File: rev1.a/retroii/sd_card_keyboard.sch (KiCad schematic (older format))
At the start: 47 parts, among them CON1 SD_Card_SPI, J22 Conn_01x09, K1 PS2_KEYBOARD, P2 PROP_PLUG, Q5 2N3904, SW3 SAVE, SW4 LOAD, SW5 SW_PUSH_SAFE, SW6 RESET, SW7 MISC1, SW8 MISC2, U16 Prop_P8X32A, U17 24LC256_EEPROM, Y3 5MHz 20pf

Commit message: added tactile switches 3d models, footprints, symbols.
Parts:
- SW3, SW4, SW6, SW7, SW8: footprint (none) -> retroii_footprints:TE_Tactile_2-1825027-0; symbol Switch:SW_Push -> retroii:SW_Push
- SW5: footprint 6502Library:1-1825027-1-TACTILE_SWITCH -> retroii_footprints:TE_1825910-6; symbol 6502:SW_PUSH_SAFE -> retroii:SW_Push
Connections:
- wire segments 254 -> 256
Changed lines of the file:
@@
 NoConn ~ 2700 1700
 $Comp
-L 6502:SW_PUSH_SAFE SW5
+L retroii:SW_Push SW5
 U 1 1 5C8ADCC7
 P 3580 1455
 F 0 "SW5" H 3730 1565 50  0000 C CNN
 F 1 "SW_PUSH_SAFE" H 3580 1375 50  0000 C CNN
-F 2 "6502Library:1-1825027-1-TACTILE_SWITCH" H 3580 1455 60  0001 C CNN
+F 2 "retroii_footprints:TE_1825910-6" H 3580 1455 60  0001 C CNN
 F 3 "" H 3580 1455 60  0000 C CNN
 	1    3580 1455
@@
 ~Reset
 $Comp
-L Switch:SW_Push SW4
+L retroii:SW_Push SW4
 U 1 1 5D8FADA2
 P 1270 3375
 F 0 "SW4" H 1270 3325 50  0000 C CNN
 F 1 "LOAD" H 1270 3530 50  0000 C CNN
-F 2 "" H 1270 3575 50  0001 C CNN
+F 2 "retroii_footprints:TE_Tactile_2-1825027-0" H 1270 3575 50  0001 C CNN
 F 3 "~" H 1270 3575 50  0001 C CNN
 	1    1270 3375
@@
 $EndComp
 $Comp
-L Switch:SW_Push SW6
+L retroii:SW_Push SW6
 U 1 1 5D8FC47F
 P 3725 5450
 F 0 "SW6" H 3735 5385 50  0000 C CNN
 F 1 "RESET" H 3725 5605 50  0000 C CNN
-F 2 "" H 3725 5650 50  0001 C CNN
+F 2 "retroii_footprints:TE_Tactile_2-1825027-0" H 3725 5650 50  0001 C CNN
 F 3 "~" H 3725 5650 50  0001 C CNN
 	1    3725 5450
@@
 	1635 3375 1700 3375
 $Comp
-L Switch:SW_Push SW3
+L retroii:SW_Push SW3
 U 1 1 5CDC6D67
 P 1270 3980
 F 0 "SW3" H 1270 3930 50  0000 C CNN
 F 1 "SAVE" H 1270 4135 50  0000 C CNN
-F 2 "" H 1270 4180 50  0001 C CNN
+F 2 "retroii_footprints:TE_Tactile_2-1825027-0" H 1270 4180 50  0001 C CNN
 F 3 "~" H 1270 4180 50  0001 C CNN
 	1    1270 3980
@@
 	1635 3980 1700 3980
 $Comp
-L Switch:SW_Push SW7
+L retroii:SW_Push SW7
 U 1 1 5CE00EDA
 P 1270 4535
 F 0 "SW7" H 1270 4485 50  0000 C CNN
 F 1 "MISC1" H 1270 4690 50  0000 C CNN
-F 2 "" H 1270 4735 50  0001 C CNN
+F 2 "retroii_footprints:TE_Tactile_2-1825027-0" H 1270 4735 50  0001 C CNN
 F 3 "~" H 1270 4735 50  0001 C CNN
 	1    1270 4535
@@
 	1635 4535 1700 4535
 $Comp
-L Switch:SW_Push SW8
+L retroii:SW_Push SW8
 U 1 1 5CE00EF8
 P 1270 5140
 F 0 "SW8" H 1270 5090 50  0000 C CNN
 F 1 "MISC2" H 1270 5295 50  0000 C CNN
-F 2 "" H 1270 5340 50  0001 C CNN
+F 2 "retroii_footprints:TE_Tactile_2-1825027-0" H 1270 5340 50  0001 C CNN
 F 3 "~" H 1270 5340 50  0001 C CNN
 	1    1270 5140
@@
 NoConn ~ 5115 6835
 NoConn ~ 5115 6935
+Wire Wire Line
+	3380 1455 3280 1455
+Wire Wire Line
+	3780 1455 3880 1455
+Connection ~ 3880 1455
 Wire Bus Line
 	10725 2260 10725 5405

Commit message: finished footprints/models for power supply caps
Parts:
- C37: footprint 6502Library:C_Disc_D6_P5 -> Capacitor_THT:C_Disc_D4.7mm_W2.5mm_P5.00mm
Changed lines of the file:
@@
 F 0 "C37" H 8500 1610 50  0000 L CNN
 F 1 "1uf" H 8500 1460 50  0000 L CNN
-F 2 "6502Library:C_Disc_D6_P5" H 8490 1540 60  0001 C CNN
+F 2 "Capacitor_THT:C_Disc_D4.7mm_W2.5mm_P5.00mm" H 8490 1540 60  0001 C CNN
 F 3 "" H 8490 1540 60  0000 C CNN
 	1    8490 1540

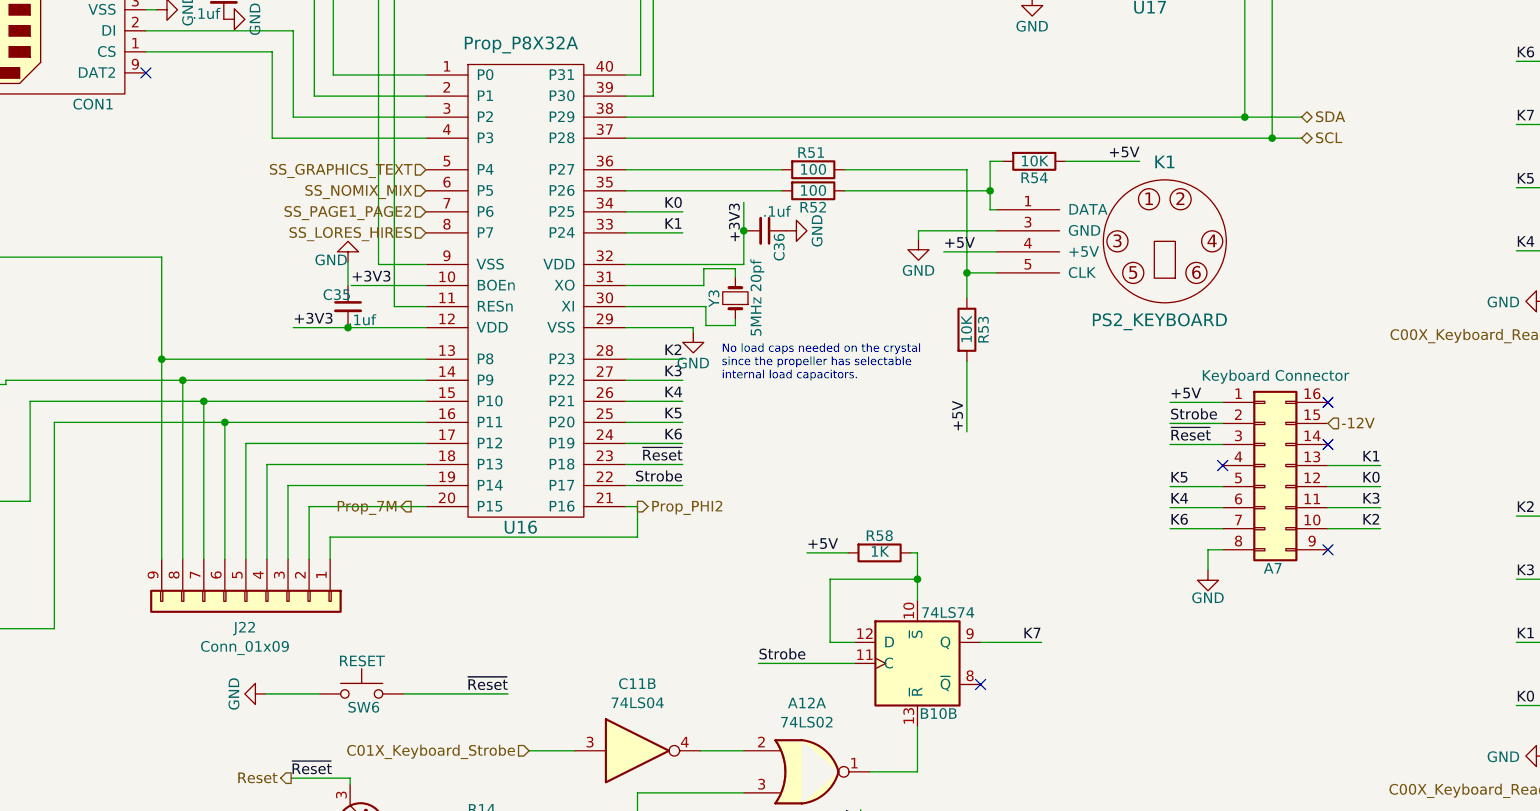
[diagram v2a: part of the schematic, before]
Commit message: added series resistors for prop 5v interface pins.
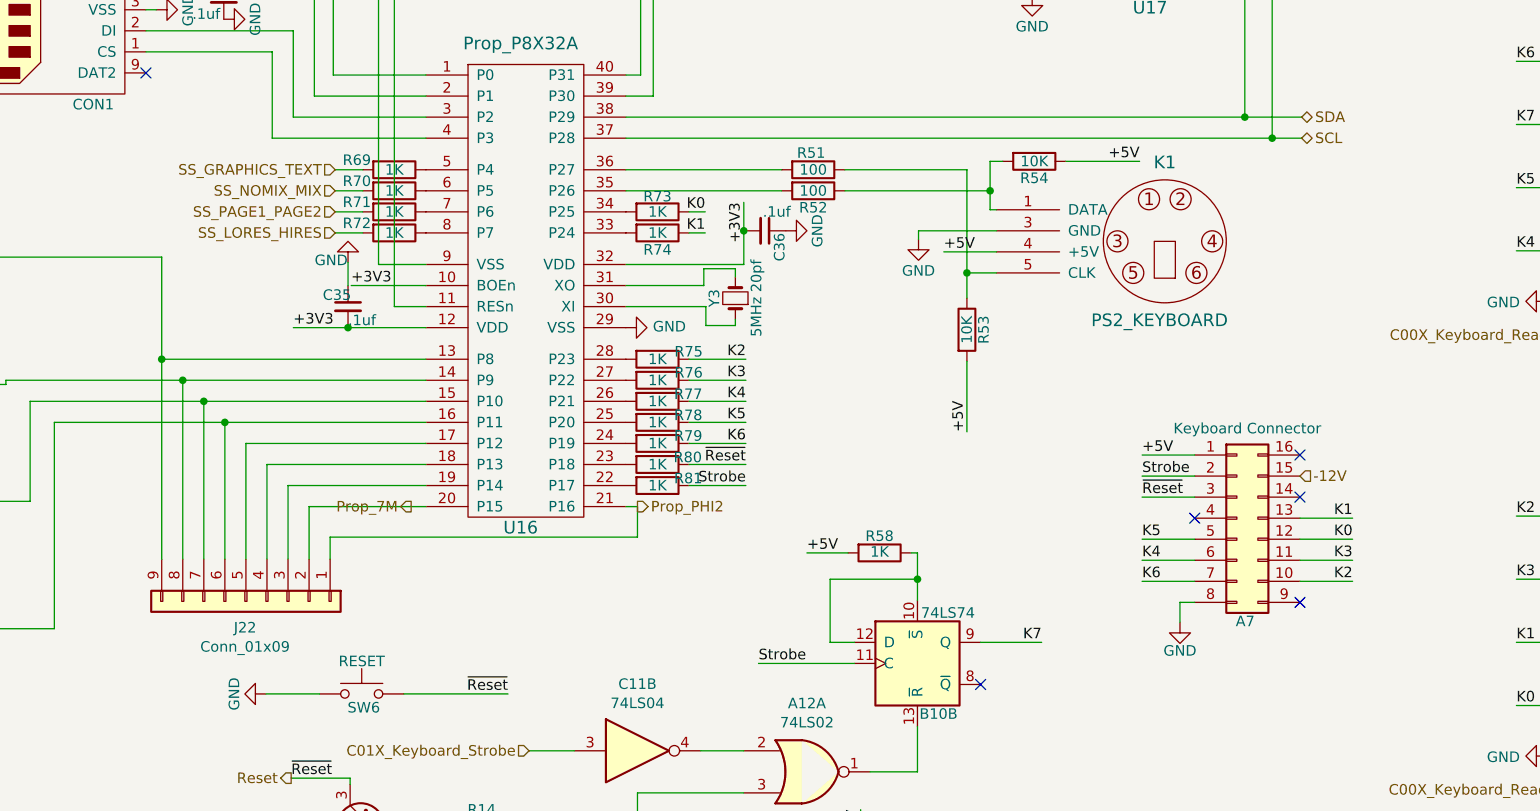
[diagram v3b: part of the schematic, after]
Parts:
- added R69, R70, R71, R72, R73, R74, R75, R76, R77, R78, R79, R80, R81: 1K, retroii_footprints:R_Axial_DIN0207_L6.3mm_D2.5mm_P10.16mm_Horizontal, symbol device:R
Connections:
- net K0: now also R73.1; no longer U16.34 (P25)
- net K1: now also R74.1; no longer U16.33 (P24)
- net K2: now also R75.1; no longer U16.28 (P23)
- net K3: now also R76.1; no longer U16.27 (P22)
- net K4: now also R77.1; no longer U16.26 (P21)
- net K5: now also R78.1; no longer U16.25 (P20)
- net K6: now also R79.1; no longer U16.24 (P19)
- net Reset: now also R80.1; no longer U16.23 (P18)
- net SS_GRAPHICS_TEXT: now also R69.2; no longer U16.5 (P4)
- net SS_LORES_HIRES: now also R72.2; no longer U16.8 (P7)
- net SS_NOMIX_MIX: now also R70.2; no longer U16.6 (P5)
- net SS_PAGE1_PAGE2: now also R71.2; no longer U16.7 (P6)
- net Strobe: now also R81.1; no longer U16.22 (P17)
- new net: R81.2, U16.22 (P17)
- new net: R80.2, U16.23 (P18)
- new net: R79.2, U16.24 (P19)
- new net: R78.2, U16.25 (P20)
- new net: R77.2, U16.26 (P21)
- new net: R76.2, U16.27 (P22)
- new net: R75.2, U16.28 (P23)
- new net: R74.2, U16.33 (P24)
- new net: R73.2, U16.34 (P25)
- new net: R69.1, U16.5 (P4)
- new net: R70.1, U16.6 (P5)
- new net: R71.1, U16.7 (P6)
- new net: R72.1, U16.8 (P7)
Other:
- note removed: "No load caps needed on the crystal\nsince the propeller has selectable\ninternal load capacitors."
- moved on the sheet: A7

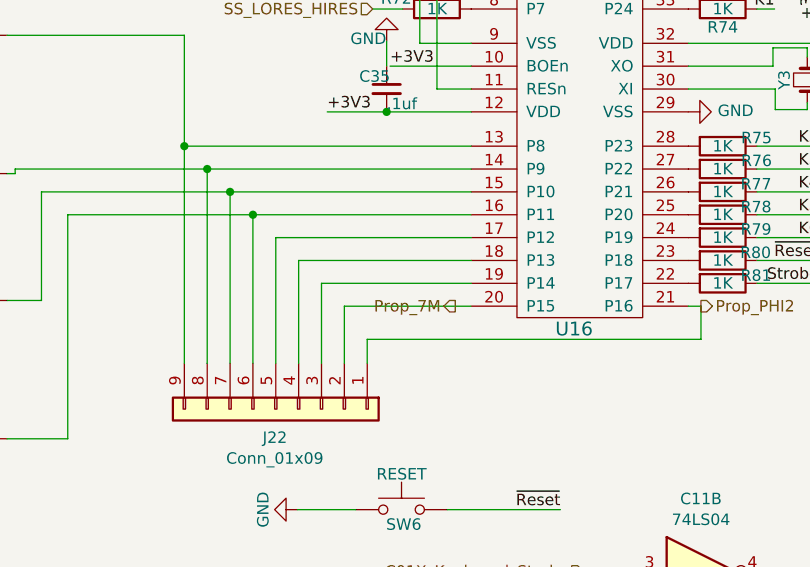
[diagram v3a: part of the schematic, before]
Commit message: added prop_q3 to peripheral slot connections.
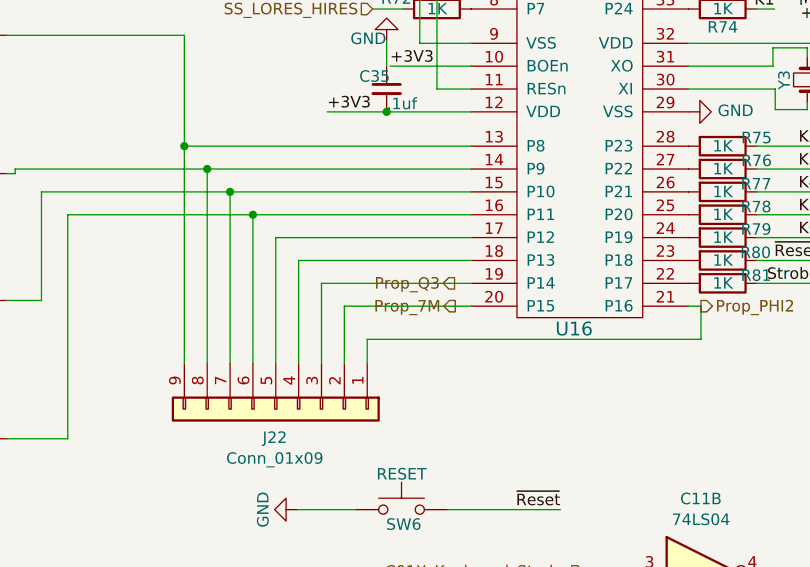
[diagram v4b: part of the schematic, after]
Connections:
- net Prop_Q3: now reaches J22.3 (Pin_3), U16.19 (P14)
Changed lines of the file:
@@
 	3375 4810 3375 4460
-Wire Wire Line
-	3375 4460 4030 4460
 Wire Wire Line
 	4980 4560 5035 4560
@@
 Wire Wire Line
 	3730 3260 3599 3260
+Text HLabel 3957 4460 0    50   Output ~ 0
+Prop_Q3
+Wire Wire Line
+	3375 4460 4030 4460
 Wire Bus Line
 	10725 2260 10725 5405

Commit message: working on optimizing keyboard layout
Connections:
- net SS_GRAPHICS_TEXT: now also R72.2; no longer R69.2
- net SS_LORES_HIRES: now also R69.2; no longer R72.2
- net SS_NOMIX_MIX: now also R71.2; no longer R70.2
- net SS_PAGE1_PAGE2: now also R70.2; no longer R71.2
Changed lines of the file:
@@
 Text HLabel 3390 5850 0    50   Output ~ 0
 Reset
+Text HLabel 3599 3260 0    50   Input ~ 0
+SS_GRAPHICS_TEXT
+Text HLabel 3599 3160 0    50   Input ~ 0
+SS_NOMIX_MIX
+Text HLabel 3599 3060 0    50   Input ~ 0
+SS_PAGE1_PAGE2
 Text HLabel 3599 2960 0    50   Input ~ 0
-SS_GRAPHICS_TEXT
-Text HLabel 3599 3060 0    50   Input ~ 0
-SS_NOMIX_MIX
-Text HLabel 3599 3160 0    50   Input ~ 0
-SS_PAGE1_PAGE2
-Text HLabel 3599 3260 0    50   Input ~ 0
 SS_LORES_HIRES
 Wire Wire Line

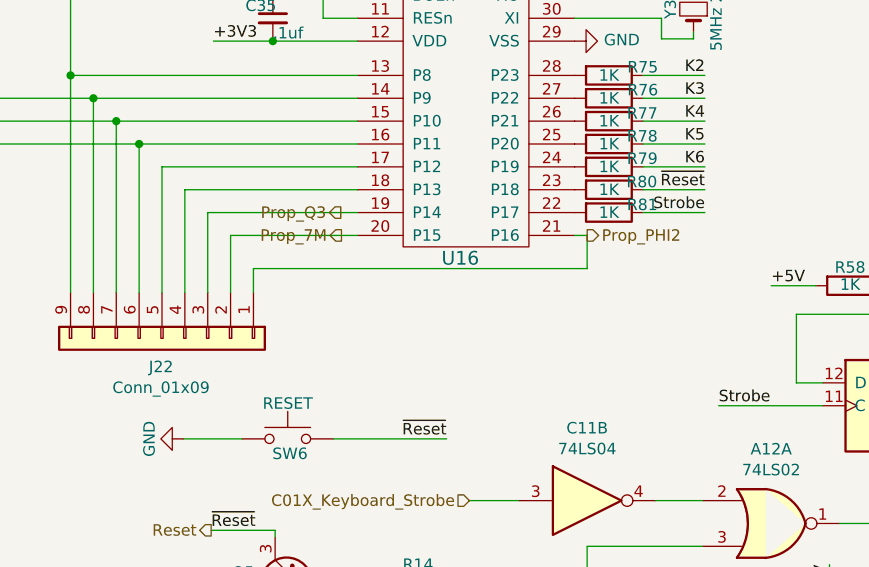
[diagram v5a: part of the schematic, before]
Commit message: modified prop layout to include jumpers for phi2, rdy, and dma.
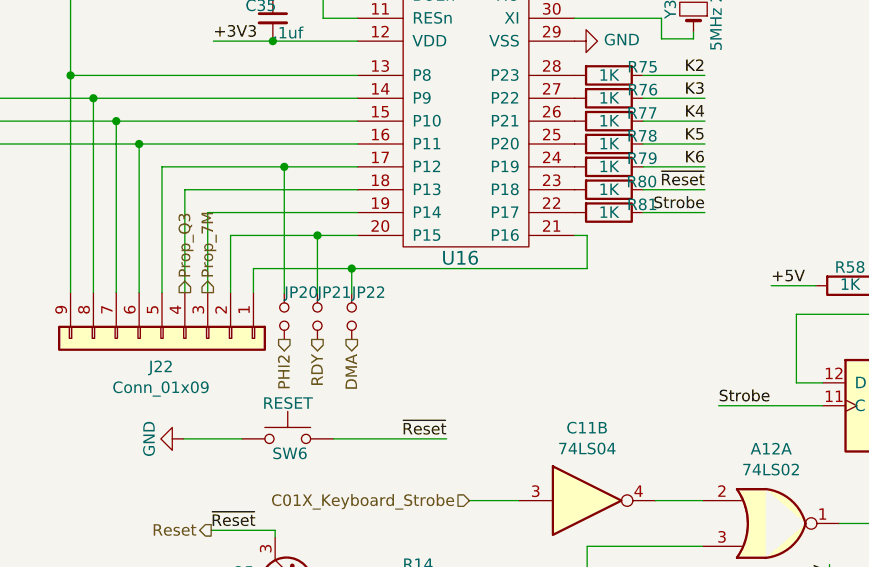
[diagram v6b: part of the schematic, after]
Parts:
- added JP20, JP21, JP22: Jumper_NO_Small, Connector_PinHeader_2.54mm:PinHeader_1x02_P2.54mm_Vertical, symbol Device:Jumper_NO_Small
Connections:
- net Prop_7M: now also J22.3 (Pin_3), U16.19 (P14); no longer J22.2 (Pin_2), U16.20 (P15)
- net Prop_Q3: now also J22.4 (Pin_4), U16.18 (P13); no longer J22.3 (Pin_3), U16.19 (P14)
- net at J22.5 (Pin_5), U16.17 (P12): now also JP20.1
- net Prop_PHI2: no longer names the net of J22.1 (Pin_1), U16.21 (P16)
- net Prop_PHI2: now also JP22.1
- new net: J22.2 (Pin_2), JP21.1, U16.20 (P15)
- new net DMA: JP22.2
- new net PHI2: JP20.2
- new net RDY: JP21.2
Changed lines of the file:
@@
 	3175 4810 3175 4260
 Wire Wire Line
-	3175 4260 4030 4260
+	3175 4260 3710 4260
 Wire Wire Line
 	4030 4360 3275 4360
@@
 	5035 4560 5035 4705
 Wire Wire Line
-	5035 4705 3575 4705
+	5035 4705 4005 4705
 Wire Wire Line
 	3575 4705 3575 4810
@@
 +5V
 Wire Wire Line
-	3475 4560 4030 4560
-Text HLabel 5035 4560 2    50   Output ~ 0
-Prop_PHI2
-Text HLabel 3960 4560 0    50   Output ~ 0
+	3475 4560 3855 4560
+Text HLabel 3375 4810 1    50   Output ~ 0
 Prop_7M
 NoConn ~ 5115 6835
@@
 Wire Wire Line
 	3730 3260 3599 3260
-Text HLabel 3957 4460 0    50   Output ~ 0
+Text HLabel 3275 4810 1    50   Output ~ 0
 Prop_Q3
 Wire Wire Line
 	3375 4460 4030 4460
+Text HLabel 3710 5015 3    50   Output ~ 0
+PHI2
+Text HLabel 3855 5015 3    50   Output ~ 0
+RDY
+Text HLabel 4005 5015 3    50   Output ~ 0
+DMA
+$Comp
+L Device:Jumper_NO_Small JP22
+U 1 1 5D7BEB06
+P 4005 4915
+F 0 "JP22" V 3900 4915 50  0000 L CNN
+F 1 "Jumper_NO_Small" V 4050 4963 50  0001 L CNN
+F 2 "Connector_PinHeader_2.54mm:PinHeader_1x02_P2.54mm_Vertical" H 4005 4915 50  0001 C CNN
+F 3 "~" H 4005 4915 50  0001 C CNN
+	1    4005 4915
+	0    1    1    0
+$EndComp
+Wire Wire Line
+	4005 4815 4005 4705
+Connection ~ 4005 4705
+Wire Wire Line
+	4005 4705 3575 4705
+$Comp
+L Device:Jumper_NO_Small JP21
+U 1 1 5D7ECAFE
+P 3855 4915
+F 0 "JP21" V 3750 4915 50  0000 L CNN
+F 1 "Jumper_NO_Small" V 3900 4963 50  0001 L CNN
+F 2 "Connector_PinHeader_2.54mm:PinHeader_1x02_P2.54mm_Vertical" H 3855 4915 50  0001 C CNN
+F 3 "~" H 3855 4915 50  0001 C CNN
+	1    3855 4915
+	0    1    1    0
+$EndComp
+Wire Wire Line
+	3855 4815 3855 4560
+Connection ~ 3855 4560
+Wire Wire Line
+	3855 4560 4030 4560
+$Comp
+L Device:Jumper_NO_Small JP20
+U 1 1 5D802F37
+P 3710 4915
+F 0 "JP20" V 3605 4915 50  0000 L CNN
+F 1 "Jumper_NO_Small" V 3755 4963 50  0001 L CNN
+F 2 "Connector_PinHeader_2.54mm:PinHeader_1x02_P2.54mm_Vertical" H 3710 4915 50  0001 C CNN
+F 3 "~" H 3710 4915 50  0001 C CNN
+	1    3710 4915
+	0    1    1    0
+$EndComp
+Wire Wire Line
+	3710 4815 3710 4260
 Wire Bus Line
 	10725 2260 10725 5405
+Connection ~ 3710 4260
+Wire Wire Line
+	3710 4260 4030 4260
 $EndSCHEMATC

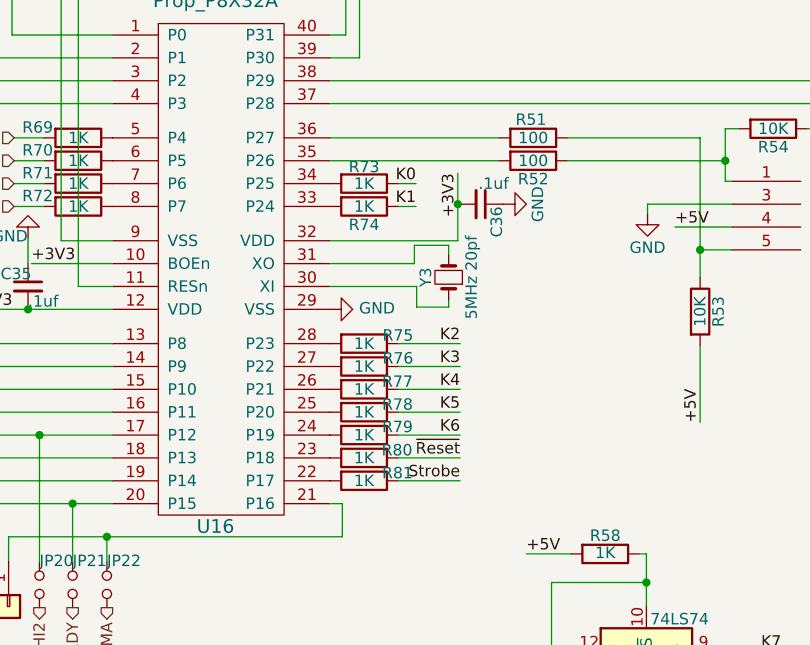
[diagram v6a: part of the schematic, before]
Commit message: updated strobe/reset/keyboard connections
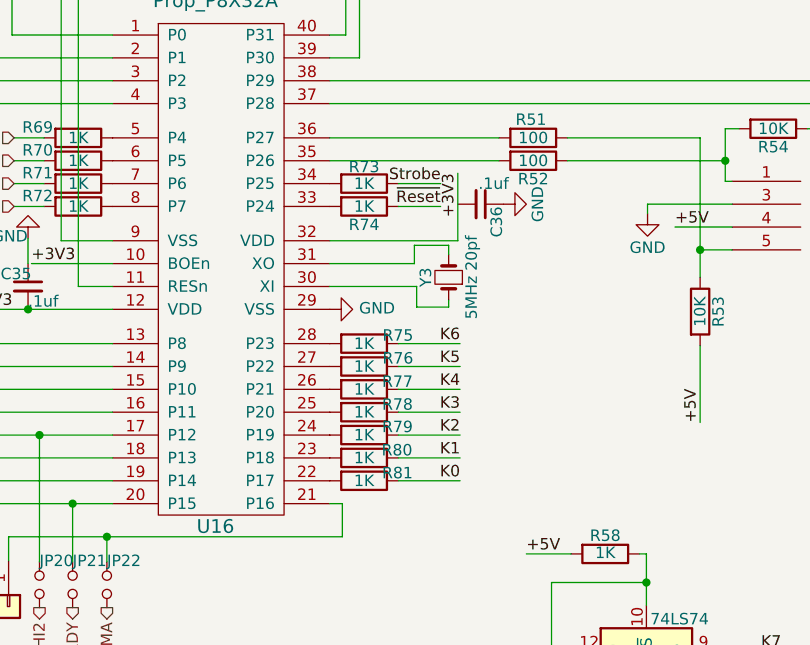
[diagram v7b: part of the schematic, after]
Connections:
- net +3V3: no longer C36.2
- net K0: now also R81.1; no longer R73.1
- net K1: now also R80.1; no longer R74.1
- net K2: now also R79.1; no longer R75.1
- net K3: now also R78.1; no longer R76.1
- net K5: now also R76.1; no longer R78.1
- net K6: now also R75.1; no longer R79.1
- net Reset: now also R74.1; no longer R80.1
- net Strobe: now also R73.1; no longer R81.1
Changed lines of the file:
@@
 	0    1    1    0
 $EndComp
-Wire Wire Line
-	5540 3410 5540 3250
 $Comp
 L device:C_Small C37
@@
 Text Label 6955 5205 2    50   ~ 0
 K7
-Text Label 5550 4460 2    50   ~ 0
+Text Label 5465 3160 2    50   ~ 0
 Strobe
-Wire Wire Line
-	5280 4460 5550 4460
-Text Label 5550 4360 2    50   ~ 0
+Text Label 5465 3260 2    50   ~ 0
 ~Reset
-Wire Wire Line
-	5280 4360 5550 4360
-Text Label 5550 4260 2    50   ~ 0
+Text Label 5550 3860 2    50   ~ 0
 K6
 Wire Wire Line
 	5280 4260 5550 4260
-Text Label 5550 4160 2    50   ~ 0
+Text Label 5550 3960 2    50   ~ 0
 K5
 Wire Wire Line
@@
 Wire Wire Line
 	5280 4060 5550 4060
-Text Label 5550 3960 2    50   ~ 0
+Text Label 5550 4160 2    50   ~ 0
 K3
 Wire Wire Line
 	5280 3960 5550 3960
-Text Label 5550 3860 2    50   ~ 0
+Text Label 5550 4260 2    50   ~ 0
 K2
 Wire Wire Line
 	5280 3860 5550 3860
-Text Label 5357 3260 2    50   ~ 0
+Text Label 5550 4360 2    50   ~ 0
 K1
-Text Label 5357 3160 2    50   ~ 0
+Text Label 5550 4460 2    50   ~ 0
 K0
 Wire Wire Line
@@
 Text Label 3675 3510 0    50   ~ 0
 +3V3
-Wire Wire Line
-	5540 3250 5540 3115
-Connection ~ 5540 3250
 Text Label 5540 3115 3    50   ~ 0
 +3V3
@@
 	5035 4560 5035 4705
 Wire Wire Line
-	5035 4705 4005 4705
-Wire Wire Line
 	3575 4705 3575 4810
 Wire Wire Line
@@
 	0    1    1    0
 $EndComp
-Wire Wire Line
-	5280 3160 5357 3160
-Wire Wire Line
-	5280 3260 5357 3260
 $Comp
 L device:R R75
@@
 	0    1    1    0
 $EndComp
-Wire Wire Line
-	4005 4815 4005 4705
-Connection ~ 4005 4705
-Wire Wire Line
-	4005 4705 3575 4705
 $Comp
 L Device:Jumper_NO_Small JP21
@@
 Wire Wire Line
 	3710 4815 3710 4260
+Connection ~ 3710 4260
+Wire Wire Line
+	3710 4260 4030 4260
+Wire Wire Line
+	5540 3115 5540 3410
+Wire Wire Line
+	5280 3160 5465 3160
+Wire Wire Line
+	5280 3260 5465 3260
+Wire Wire Line
+	5280 4460 5550 4460
+Wire Wire Line
+	5280 4360 5550 4360
+Wire Wire Line
+	4005 4815 4005 4705
+Wire Wire Line
+	4005 4705 3575 4705
+Connection ~ 4005 4705
+Wire Wire Line
+	5035 4705 4005 4705
 Wire Bus Line
 	10725 2260 10725 5405
-Connection ~ 3710 4260
-Wire Wire Line
-	3710 4260 4030 4260
 $EndSCHEMATC
